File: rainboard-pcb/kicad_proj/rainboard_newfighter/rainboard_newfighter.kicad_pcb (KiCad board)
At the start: 2 copper layers, 260 x 253.6 mm, 595 parts, among them J1 EJ508A, J10 Conn_01x03, J11 SDS-50J, J12 SDS-50J, J13 Conn_01x02, J14 Conn_01x02, J15 Conn_01x02, J16 Conn_01x02, J2 Conn_01x02, J3 Conn_01x03, J4 Conn_01x03, J5 Conn_01x02, J6 Conn_01x02, J6 SDS-50J, J7 Conn_01x02, J7 SDS-50J, J8 Conn_01x02, Q1 DUAL 30V NMOS, Q2 DUAL 30V NMOS, Q3 30V 10mOhm, U1 RT8298, U2 ATmega16U2-MU, U3 6N138SDM, U4 74HC14, U5 ATmega16U2-MU, U6 ATmega2560-16AU, Y1 16MHz, Y1 Crystal, Y2 16MHz, Y2 Crystal, Y3 16MHz

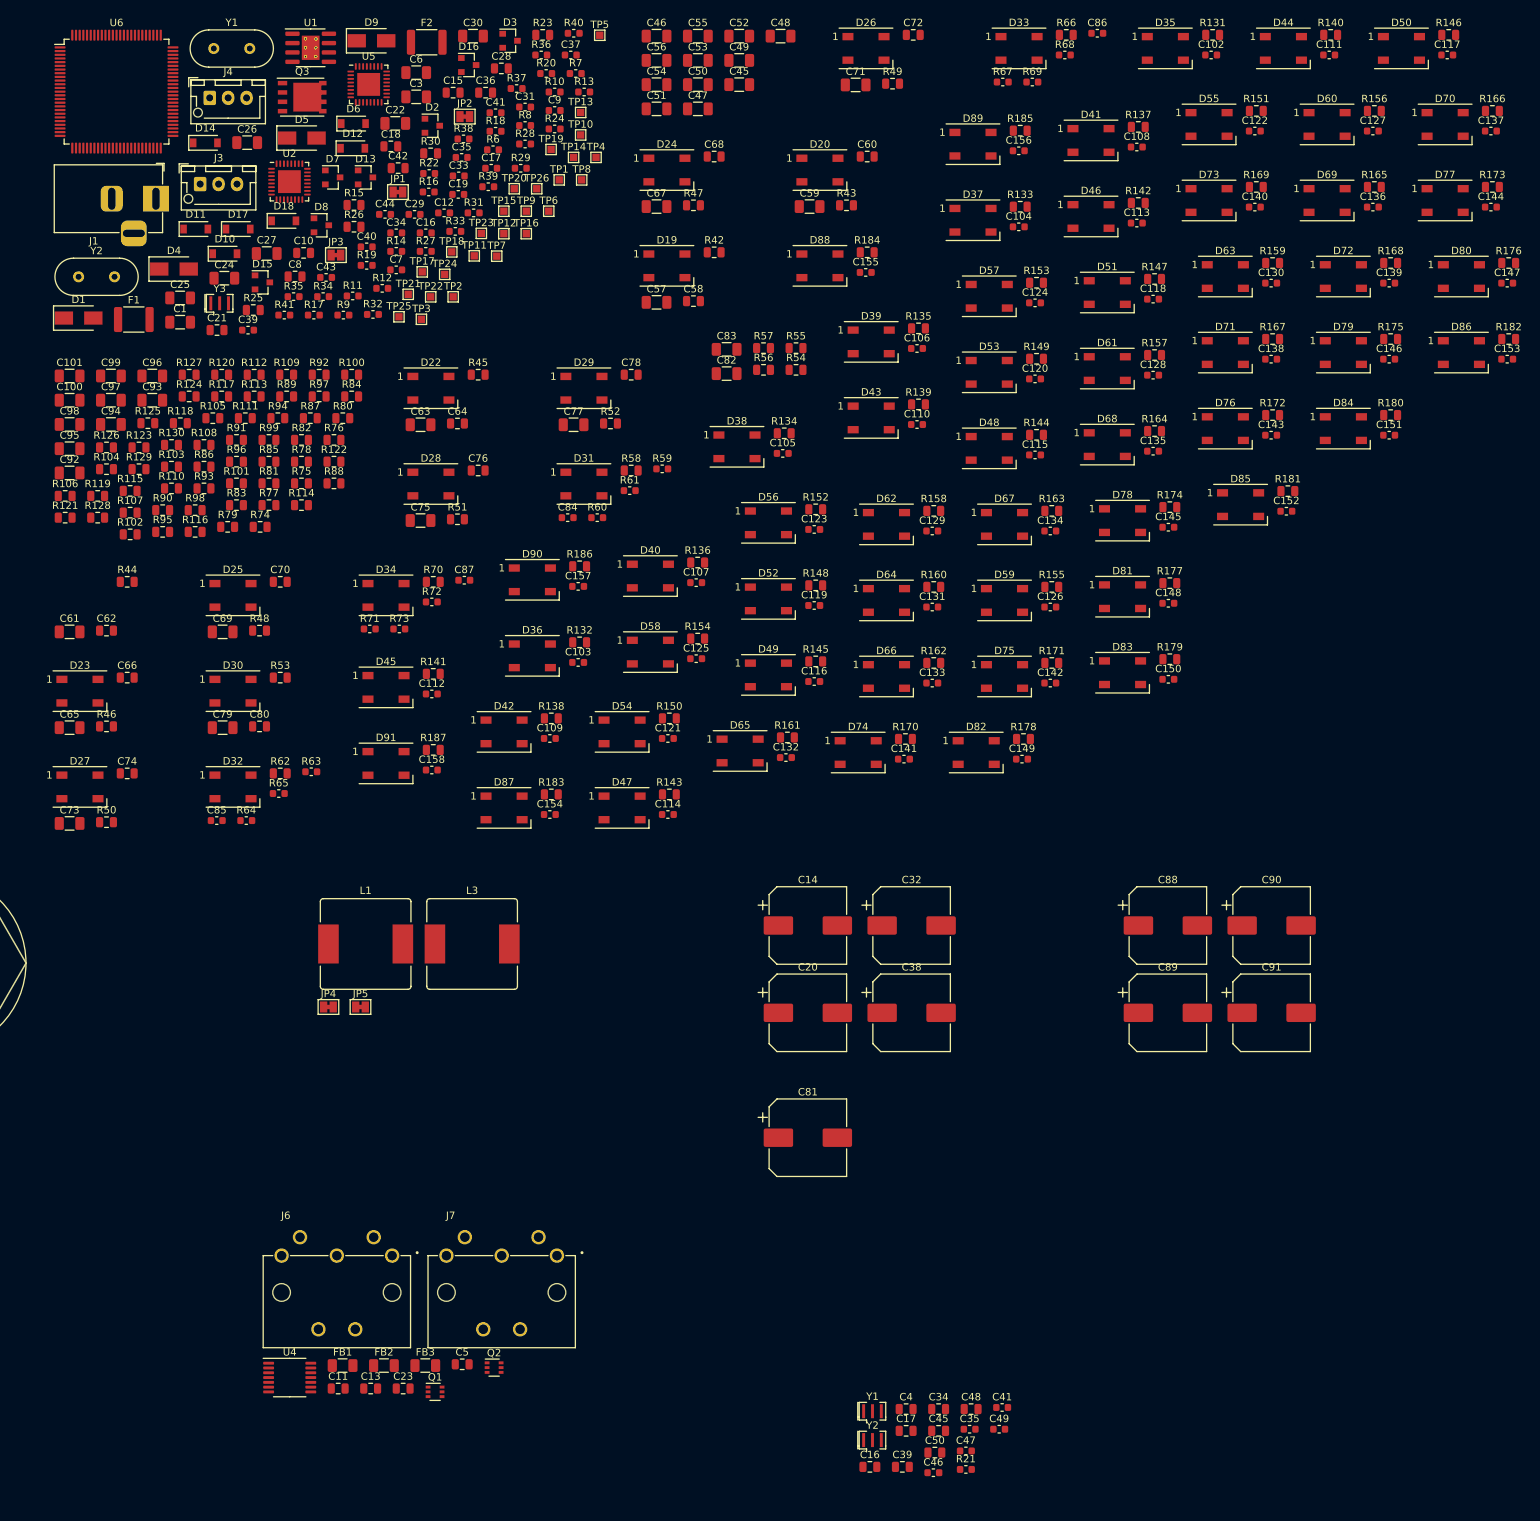
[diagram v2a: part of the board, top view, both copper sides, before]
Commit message: New footprints added
Updated library format for footprints. Pending sync with layout to add all new footprints
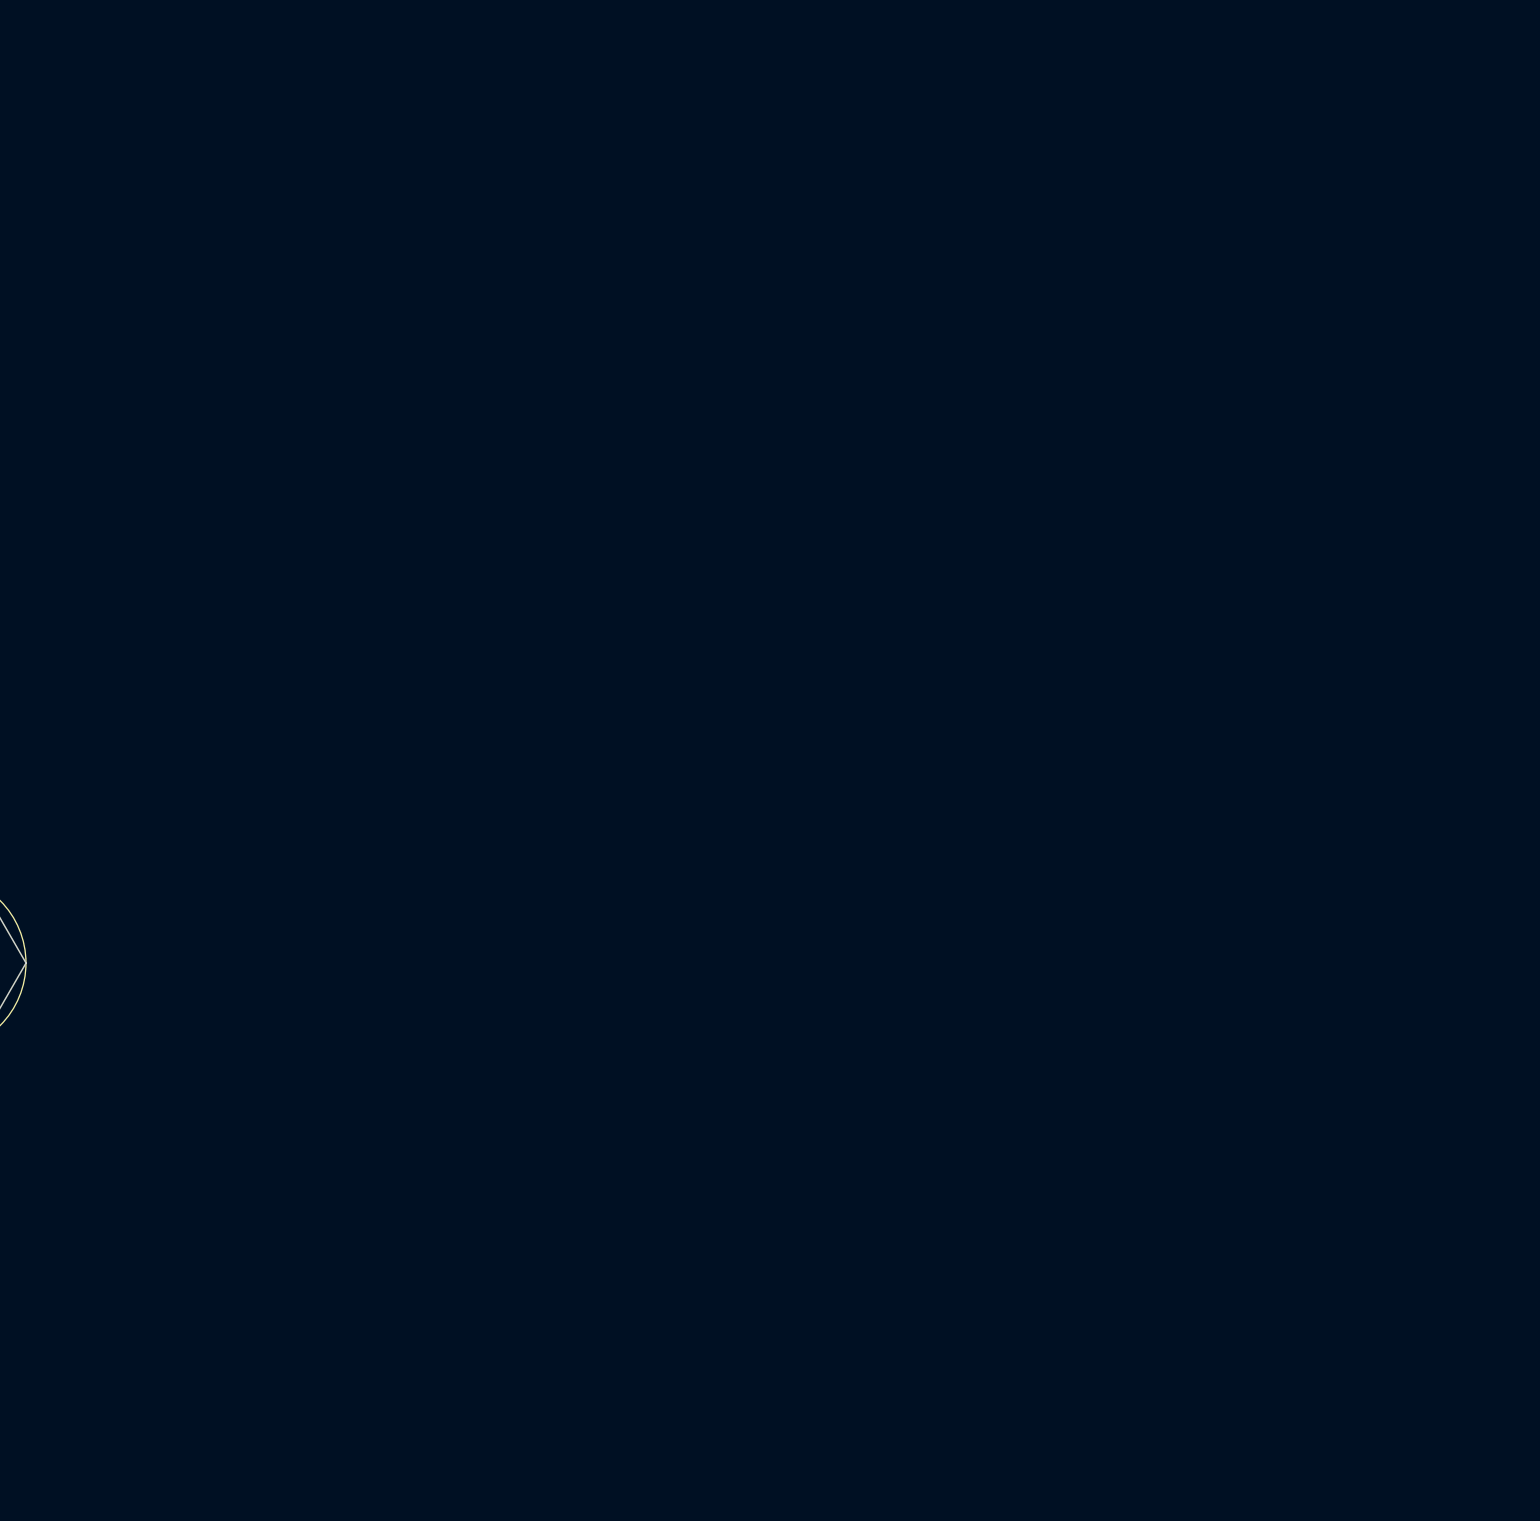
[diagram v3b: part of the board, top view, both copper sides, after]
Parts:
- removed the C1 at (150.9, -87.0)
- removed C10, C11, C13, C15, C17, C18, C21, C23, C28, C34, C36, C39, C42, C45, C48, C5, C50, C58, C60, C62, C64, C66, C68, C70, C72, C74, C76, C78, C8, C80: 1uF 25V, Capacitor_SMD:C_0805_2012Metric
- removed C100, C101, C22, C24, C25, C26, C27, C30, C45, C46, C47, C48, C49, C50, C51, C52, C53, C54, C55, C56, C6, C82, C83, C92, C93, C94, C95, C96, C97, C98, C99: 10uF 25V, Capacitor_SMD:C_1206_3216Metric
- removed C102, C103, C104, C105, C106, C107, C108, C109, C110, C111, C112, C113, C114, C115, C116, C117, C118, C119, C12, C120, C121, C122, C123, C124, C125, C126, C127, C128, C129, C130, C131, C132, C133, C134, C135, C136, C137, C138, C139, C140, C141, C142, C143, C144, C145, C146, C147, C148, C149, C150, C151, C152, C153, C154, C155, C156, C157, C158, C19, C29, C31, C33, C35, C37, C39, C40, C41 (x2), C43, C44, C46, C47, C49, C7, C84, C85, C86, C87, C9: 100nf, Capacitor_SMD:C_0603_1608Metric
- removed C14, C20, C32, C38, C81, C88, C89, C90, C91: 470uF 25V, Capacitor_SMD:CP_Elec_10x10
- removed C16: DNP-1uF 25V, Capacitor_SMD:C_0805_2012Metric
- removed C16, C17, C34, C35: 22PF, Capacitor_SMD:C_0603_1608Metric
- removed the C3 at (182.9, -117.6)
- removed the C4 at (249.4, 60.5)
- removed C57, C59, C61, C63, C65, C67, C69, C71, C73, C75, C77, C79: DNP-10uF 25V, Capacitor_SMD:C_1206_3216Metric
- removed the D1 at (137.1, -87.5)
- removed D10, D11, D12, D14, D17, D18, D6: 40V 1A, Diode_SMD:D_SOD-123
- removed D13, D15, D16, D2, D3, D7, D8: 5Vw, Package_TO_SOT_SMD:SOT-23
- removed D19, D20, D22, D23, D24, D25, D26, D27, D28, D29, D30, D31, D32, D33, D34, D35, D36, D37, D38, D39, D40, D41, D42, D43, D44, D45, D46, D47, D48, D49, D50, D51, D52, D53, D54, D55, D56, D57, D58, D59, D60, D61, D62, D63, D64, D65, D66, D67, D68, D69, D70, D71, D72, D73, D74, D75, D76, D77, D78, D79, D80, D81, D82, D83, D84, D85, D86, D87, D88, D89, D90, D91: WS2812B, LED_SMD:LED_WS2812B_PLCC4_5.0x5.0mm_P3.2mm
- removed D4, D9: 5Vw, Diode_SMD:D_SMA
- removed D5: 12Vw, Diode_SMD:D_SMA
- removed F1: 20V 3A, Fuse:Fuse_1812_4532Metric
- removed F2: 15V .5A, Fuse:Fuse_1812_4532Metric
- removed FB1, FB2, FB3: 4A Ferrite, Inductor_SMD:L_1206_3216Metric
- removed the J1 at (147.6, -103.7)
- removed the J3 at (153.6, -105.7)
- removed the J4 at (154.9, -117.4)
- removed the J6 at (172.2, 39.7)
- removed the J7 at (194.5, 39.7)
- removed JP1, JP2, JP3, JP4, JP5: Jumper, Jumper:SolderJumper-2_P1.3mm_Bridged_Pad1.0x1.5mm
- removed L1, L3: 27uH, Inductor_SMD:L_Bourns_SRR1210A
- removed Q1, Q2: DUAL 30V NMOS, Package_TO_SOT_SMD:SOT-363_SC-70-6
- removed Q3: 30V 10mOhm, Package_SO:PowerPAK_SO-8_Single
- removed the R10 at (201.7, -118.2)
- removed R100, R101, R102, R103, R104, R105, R106, R107, R108, R109, R110, R111, R112, R113, R114, R115, R116, R117, R118, R119, R120, R121, R122, R123, R124, R125, R126, R127, R128, R129, R130, R131, R132, R133, R134, R135, R136, R137, R138, R139, R140, R141, R142, R143, R144, R145, R146, R147, R148, R149, R15, R150, R151, R152, R153, R154, R155, R156, R157, R158, R159, R160, R161, R162, R163, R164, R165, R166, R167, R168, R169, R170, R171, R172, R173, R174, R175, R176, R177, R178, R179, R180, R181, R182, R183, R184, R185, R186, R187, R23, R25, R30, R54, R55, R56, R57, R58, R62, R66, R70, R74, R75, R76, R77, R78, R79, R80, R81, R82, R83, R84, R85, R86, R87, R88, R89, R90, R91, R92, R93, R94, R95, R96, R97, R98, R99: 210R, Resistor_SMD:R_0805_2012Metric
- removed the R11 at (174.3, -90.5)
- removed R12, R14, R16: 100k, Resistor_SMD:R_0603_1608Metric
- removed R13, R24, R27, R28, R34, R40, R60, R61, R64, R65, R68, R69, R72, R73: 19.1k, Resistor_SMD:R_0603_1608Metric
- removed R17, R20, R22, R29, R31, R36, R37, R38, R39, R8: 11R, Resistor_SMD:R_0603_1608Metric
- removed R18: DNP-4.7k, Resistor_SMD:R_0603_1608Metric
- removed R19, R32, R33, R35, R41, R59, R63, R67, R71: 4.7k, Resistor_SMD:R_0603_1608Metric
- removed the R21 at (257.5, 68.7)
- removed R26: DNP-210R, Resistor_SMD:R_0805_2012Metric
- removed R42, R43, R44, R45, R46, R47, R48, R49, R50, R51, R52, R53: 220R, Resistor_SMD:R_0805_2012Metric
- removed the R6 at (193.4, -110.4)
- removed the R7 at (204.6, -120.7)
- removed the R9 at (173.1, -87.9)
- removed TP1, TP10, TP11, TP12, TP13, TP14, TP15, TP16, TP17, TP18, TP19, TP2, TP20, TP21, TP22, TP23, TP24, TP25, TP26, TP3, TP4, TP5, TP6, TP7, TP8, TP9: TestPoint, TestPoint:TestPoint_Pad_1.0x1.0mm
- removed the U1 at (168.6, -124.2)
- removed the U2 at (165.7, -106.0)
- removed U4: 74HC14, Package_SO:TSSOP-14_4.4x5mm_P0.65mm
- removed U5: ATmega16U2-MU, Package_DFN_QFN:QFN-32-1EP_5x5mm_P0.5mm_EP3.1x3.1mm
- removed U6: ATmega2560-16AU, Package_QFP:TQFP-100_14x14mm_P0.5mm
- removed Y1, Y2, Y3: 16MHz, Crystal:Resonator_SMD_muRata_CSTxExxV-3Pin_3.0x1.1mm
- removed Y1, Y2: Crystal, Crystal:Crystal_HC49-U_Vertical

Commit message: Fixing annotations for buttons and meta buttons
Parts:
- removed D21: WS2812B, LED_SMD:LED_WS2812B_PLCC4_5.0x5.0mm_P3.2mm
- removed Je: Conn_01x03, Connector_JST:JST_XH_B3B-XH-AM_1x03_P2.50mm_Vertical
- removed XA1: Arduino_Mega2560_Shield, arduno_mega:Arduino_Mega2560_Shield
- added C10: 1uF 25V, Capacitor_SMD:C_0805_2012Metric, F.Cu at (258.8, -59.7)
- added C100: 10uF 25V, Capacitor_SMD:C_1206_3216Metric, F.Cu at (169.3, 8.35)
- added C101: 10uF 25V, Capacitor_SMD:C_1206_3216Metric, F.Cu at (175.0, 5.06)
- added C102: 100nf, Capacitor_SMD:C_0603_1608Metric, F.Cu at (330.4, 11.5)
- added C103: 100nf, Capacitor_SMD:C_0603_1608Metric, F.Cu at (412.2, -47.7)
- added C104: 100nf, Capacitor_SMD:C_0603_1608Metric, F.Cu at (380.7, -18.1)
- added C105: 100nf, Capacitor_SMD:C_0603_1608Metric, F.Cu at (218.6, 129.4)
- added C106: 100nf, Capacitor_SMD:C_0603_1608Metric, F.Cu at (268.9, 93.5)
- added C107: 100nf, Capacitor_SMD:C_0603_1608Metric, F.Cu at (462.5, -77.3)
- added C108: 100nf, Capacitor_SMD:C_0603_1608Metric, F.Cu at (319.2, 41.1)
- added C109: 100nf, Capacitor_SMD:C_0603_1608Metric, F.Cu at (380.7, 11.5)
- added C11: 1uF 25V, Capacitor_SMD:C_0805_2012Metric, F.Cu at (234.3, -34.9)
- added C110: 100nf, Capacitor_SMD:C_0603_1608Metric, F.Cu at (319.2, 70.7)
- added C111: 100nf, Capacitor_SMD:C_0603_1608Metric, F.Cu at (268.9, 123.1)
- added C112: 100nf, Capacitor_SMD:C_0603_1608Metric, F.Cu at (462.5, -47.7)
- added C113: 100nf, Capacitor_SMD:C_0603_1608Metric, F.Cu at (168.3, 40.6)
- added C114: 100nf, Capacitor_SMD:C_0603_1608Metric, F.Cu at (431.0, -18.1)
- added C115: 100nf, Capacitor_SMD:C_0603_1608Metric, F.Cu at (512.8, -77.3)
- added C116: 100nf, Capacitor_SMD:C_0603_1608Metric, F.Cu at (319.2, 100.3)
- added C117: 100nf, Capacitor_SMD:C_0603_1608Metric, F.Cu at (431.0, 11.5)
- added C118: 100nf, Capacitor_SMD:C_0603_1608Metric, F.Cu at (369.5, 70.7)
- added C119: 100nf, Capacitor_SMD:C_0603_1608Metric, F.Cu at (512.8, -47.7)
- added C12: 100nf, Capacitor_SMD:C_0603_1608Metric, F.Cu at (225.1, -19.6)
- added C120: 100nf, Capacitor_SMD:C_0603_1608Metric, F.Cu at (319.2, 129.9)
- added C121: 100nf, Capacitor_SMD:C_0603_1608Metric, F.Cu at (481.3, -18.1)
- added C122: 100nf, Capacitor_SMD:C_0603_1608Metric, F.Cu at (419.8, 41.1)
- added C123: 100nf, Capacitor_SMD:C_0603_1608Metric, F.Cu at (563.1, -77.3)
- added C124: 100nf, Capacitor_SMD:C_0603_1608Metric, F.Cu at (369.5, 100.3)
- added C125: 100nf, Capacitor_SMD:C_0603_1608Metric, F.Cu at (481.3, 11.5)
- added C126: 100nf, Capacitor_SMD:C_0603_1608Metric, F.Cu at (419.8, 70.7)
- added C127: 100nf, Capacitor_SMD:C_0603_1608Metric, F.Cu at (563.1, -47.7)
- added C128: 100nf, Capacitor_SMD:C_0603_1608Metric, F.Cu at (369.5, 41.1)
- added C129: 100nf, Capacitor_SMD:C_0603_1608Metric, F.Cu at (470.1, 41.1)
- added C13: 1uF 25V, Capacitor_SMD:C_0805_2012Metric, F.Cu at (238.8, -37.9)
- added C130: 100nf, Capacitor_SMD:C_0603_1608Metric, F.Cu at (531.6, -18.1)
- added C131: 100nf, Capacitor_SMD:C_0603_1608Metric, F.Cu at (419.8, 100.3)
- added C132: 100nf, Capacitor_SMD:C_0603_1608Metric, F.Cu at (531.6, 11.5)
- added C133: 100nf, Capacitor_SMD:C_0603_1608Metric, F.Cu at (470.1, 70.7)
- added C134: 100nf, Capacitor_SMD:C_0603_1608Metric, F.Cu at (419.8, 129.9)
- added C135: 100nf, Capacitor_SMD:C_0603_1608Metric, F.Cu at (520.4, 41.1)
- added C136: 100nf, Capacitor_SMD:C_0603_1608Metric, F.Cu at (470.1, 100.3)
- added C137: 100nf, Capacitor_SMD:C_0603_1608Metric, F.Cu at (520.4, 70.7)
- added C138: 100nf, Capacitor_SMD:C_0603_1608Metric, F.Cu at (470.1, 129.9)
- added C139: 100nf, Capacitor_SMD:C_0603_1608Metric, F.Cu at (570.6, 41.1)
- added C14: 470uF 25V, Capacitor_SMD:CP_Elec_10x10, F.Cu at (231.8, -72.6)
- added C140: 100nf, Capacitor_SMD:C_0603_1608Metric, F.Cu at (520.4, 100.3)
- added C141: 100nf, Capacitor_SMD:C_0603_1608Metric, F.Cu at (570.6, 70.7)
- added C142: 100nf, Capacitor_SMD:C_0603_1608Metric, F.Cu at (369.5, 129.9)
- added C143: 100nf, Capacitor_SMD:C_0603_1608Metric, F.Cu at (311.7, -77.3)
- added C144: 100nf, Capacitor_SMD:C_0603_1608Metric, F.Cu at (229.9, 4.67)
- added C145: 100nf, Capacitor_SMD:C_0603_1608Metric, F.Cu at (311.7, -47.7)
- added C146: 100nf, Capacitor_SMD:C_0603_1608Metric, F.Cu at (218.6, 40.6)
- added C147: 100nf, Capacitor_SMD:C_0603_1608Metric, F.Cu at (168.3, 70.2)
- added C148: 100nf, Capacitor_SMD:C_0603_1608Metric, F.Cu at (361.9, -77.3)
- added C149: 100nf, Capacitor_SMD:C_0603_1608Metric, F.Cu at (168.3, 99.8)
- added C15: 1uF 25V, Capacitor_SMD:C_0805_2012Metric, F.Cu at (223.4, -27.9)
- added C150: 100nf, Capacitor_SMD:C_0603_1608Metric, F.Cu at (280.2, 4.67)
- added C151: 100nf, Capacitor_SMD:C_0603_1608Metric, F.Cu at (218.6, 70.2)
- added C152: 100nf, Capacitor_SMD:C_0603_1608Metric, F.Cu at (361.9, -47.7)
- added C153: 100nf, Capacitor_SMD:C_0603_1608Metric, F.Cu at (168.3, 129.4)
- added C154: 100nf, Capacitor_SMD:C_0603_1608Metric, F.Cu at (268.9, 34.3)
- added C155: 100nf, Capacitor_SMD:C_0603_1608Metric, F.Cu at (412.2, -77.3)
- added C156: 100nf, Capacitor_SMD:C_0603_1608Metric, F.Cu at (268.9, 63.9)
- added C157: 100nf, Capacitor_SMD:C_0603_1608Metric, F.Cu at (218.6, 99.8)
- added C158: 100nf, Capacitor_SMD:C_0603_1608Metric, F.Cu at (330.4, -18.1)
- added C16: DNP-1uF 25V, Capacitor_SMD:C_0805_2012Metric, F.Cu at (233.8, -31.3)
- added C17: 1uF 25V, Capacitor_SMD:C_0805_2012Metric, F.Cu at (220.9, -21.3)
- added C18: 1uF 25V, Capacitor_SMD:C_0805_2012Metric, F.Cu at (247.7, -47.0)
- added C19: 100nf, Capacitor_SMD:C_0603_1608Metric, F.Cu at (213.2, -9.86)
- added C20: 470uF 25V, Capacitor_SMD:CP_Elec_10x10, F.Cu at (165.2, -17.3)
- added C21: 1uF 25V, Capacitor_SMD:C_0805_2012Metric, F.Cu at (215.7, -15.1)
- added C22: 10uF 25V, Capacitor_SMD:C_1206_3216Metric, F.Cu at (249.3, -56.0)
- added C23: 1uF 25V, Capacitor_SMD:C_0805_2012Metric, F.Cu at (258.8, -56.8)
- added C24: 10uF 25V, Capacitor_SMD:C_1206_3216Metric, F.Cu at (236.5, -44.5)
- added C25: 10uF 25V, Capacitor_SMD:C_1206_3216Metric, F.Cu at (249.3, -59.3)
- added C26: 10uF 25V, Capacitor_SMD:C_1206_3216Metric, F.Cu at (224.4, -34.9)
- added C27: 10uF 25V, Capacitor_SMD:C_1206_3216Metric, F.Cu at (218.4, -27.7)
- added C28: 1uF 25V, Capacitor_SMD:C_0805_2012Metric, F.Cu at (199.1, -36.6)
- added C29: 100nf, Capacitor_SMD:C_0603_1608Metric, F.Cu at (263.0, -57.9)
- added C30: 10uF 25V, Capacitor_SMD:C_1206_3216Metric, F.Cu at (224.4, -31.6)
- added C31: 100nf, Capacitor_SMD:C_0603_1608Metric, F.Cu at (232.0, -26.1)
- added C32: 470uF 25V, Capacitor_SMD:CP_Elec_10x10, F.Cu at (179.3, -15.7)
- added C33: 100nf, Capacitor_SMD:C_0603_1608Metric, F.Cu at (217.4, -35.3)
- added C34: 1uF 25V, Capacitor_SMD:C_0805_2012Metric, F.Cu at (247.7, -49.9)
- added C35: 100nf, Capacitor_SMD:C_0603_1608Metric, F.Cu at (216.7, -12.4)
- added C36: 1uF 25V, Capacitor_SMD:C_0805_2012Metric, F.Cu at (260.4, -62.7)
- added C37: 100nf, Capacitor_SMD:C_0603_1608Metric, F.Cu at (238.6, -35.2)
- added C38: 470uF 25V, Capacitor_SMD:CP_Elec_10x10, F.Cu at (208.7, -39.8)
- added C39: 1uF 25V, Capacitor_SMD:C_0805_2012Metric, F.Cu at (229.4, -31.3)
- added C40: 100nf, Capacitor_SMD:C_0603_1608Metric, F.Cu at (232.0, -28.6)
- added C41: 100nf, Capacitor_SMD:C_0603_1608Metric, F.Cu at (203.3, -0.98)
- added C42: 1uF 25V, Capacitor_SMD:C_0805_2012Metric, F.Cu at (204.6, -6.66)
- added C43: 100nf, Capacitor_SMD:C_0603_1608Metric, F.Cu at (251.9, -47.2)
- added C44: 100nf, Capacitor_SMD:C_0603_1608Metric, F.Cu at (243.0, -38.6)
- added C45: 1uF 25V, Capacitor_SMD:C_0805_2012Metric, F.Cu at (223.4, -24.9)
- added C46: 100nf, Capacitor_SMD:C_0603_1608Metric, F.Cu at (256.3, -50.1)
- added C47: 100nf, Capacitor_SMD:C_0603_1608Metric, F.Cu at (212.7, -12.4)
- added C48: 1uF 25V, Capacitor_SMD:C_0805_2012Metric, F.Cu at (208.5, -12.4)
- added C49: 100nf, Capacitor_SMD:C_0603_1608Metric, F.Cu at (238.6, -32.6)
- added C5: 1uF 25V, Capacitor_SMD:C_0805_2012Metric, F.Cu at (252.1, -49.9)
- added C50: 1uF 25V, Capacitor_SMD:C_0805_2012Metric, F.Cu at (252.2, -52.9)
- added C6: 10uF 25V, Capacitor_SMD:C_1206_3216Metric, F.Cu at (211.4, -19.5)
- added C7: 100nf, Capacitor_SMD:C_0603_1608Metric, F.Cu at (219.9, -15.0)
- added C8: 1uF 25V, Capacitor_SMD:C_0805_2012Metric, F.Cu at (268.8, -68.0)
- added C88: 470uF 25V, Capacitor_SMD:CP_Elec_10x10, F.Cu at (140.1, 9.34)
- added C89: 470uF 25V, Capacitor_SMD:CP_Elec_10x10, F.Cu at (140.1, 21.2)
- added C9: 100nf, Capacitor_SMD:C_0603_1608Metric, F.Cu at (213.2, -7.35)
- added C90: 470uF 25V, Capacitor_SMD:CP_Elec_10x10, F.Cu at (154.2, 21.2)
- added C91: 470uF 25V, Capacitor_SMD:CP_Elec_10x10, F.Cu at (154.2, 9.34)
- added C92: 10uF 25V, Capacitor_SMD:C_1206_3216Metric, F.Cu at (163.7, 5.06)
- added C93: 10uF 25V, Capacitor_SMD:C_1206_3216Metric, F.Cu at (135.6, 32.0)
- added C94: 10uF 25V, Capacitor_SMD:C_1206_3216Metric, F.Cu at (141.2, 28.8)
- added C95: 10uF 25V, Capacitor_SMD:C_1206_3216Metric, F.Cu at (141.2, 32.0)
- added C96: 10uF 25V, Capacitor_SMD:C_1206_3216Metric, F.Cu at (169.3, 5.06)
- added C97: 10uF 25V, Capacitor_SMD:C_1206_3216Metric, F.Cu at (163.7, 8.35)
- added C98: 10uF 25V, Capacitor_SMD:C_1206_3216Metric, F.Cu at (163.7, 11.6)
- added C99: 10uF 25V, Capacitor_SMD:C_1206_3216Metric, F.Cu at (135.6, 28.8)
- added D10: 40V 1A, Diode_SMD:D_SOD-123, F.Cu at (183.1, -41.0)
- added D11: 40V 1A, Diode_SMD:D_SOD-123, F.Cu at (135.7, -1.49)
- added D12: 40V 1A, Diode_SMD:D_SOD-123, F.Cu at (152.9, -1.49)
- added D13: 5Vw, Package_TO_SOT_SMD:SOT-23, F.Cu at (216.4, -18.9)
- added D14: 40V 1A, Diode_SMD:D_SOD-123, F.Cu at (147.2, -1.49)
- added D15: 5Vw, Package_TO_SOT_SMD:SOT-23, F.Cu at (242.9, -46.0)
- added D16: 5Vw, Package_TO_SOT_SMD:SOT-23, F.Cu at (199.1, -2.06)
- added D17: 40V 1A, Diode_SMD:D_SOD-123, F.Cu at (183.1, -37.6)
- added D18: 40V 1A, Diode_SMD:D_SOD-123, F.Cu at (250.9, -62.6)
- added D2: 5Vw, Package_TO_SOT_SMD:SOT-23, F.Cu at (199.1, -40.4)
- added D3: 5Vw, Package_TO_SOT_SMD:SOT-23, F.Cu at (254.3, -58.6)
- added D35: WS2812B, LED_SMD:LED_WS2812B_PLCC4_5.0x5.0mm_P3.2mm, F.Cu at (324.2, 13.6)
- added D36: WS2812B, LED_SMD:LED_WS2812B_PLCC4_5.0x5.0mm_P3.2mm, F.Cu at (406.0, -45.6)
- added D37: WS2812B, LED_SMD:LED_WS2812B_PLCC4_5.0x5.0mm_P3.2mm, F.Cu at (374.5, -16.0)
- added D38: WS2812B, LED_SMD:LED_WS2812B_PLCC4_5.0x5.0mm_P3.2mm, F.Cu at (212.4, 131.5)
- added D39: WS2812B, LED_SMD:LED_WS2812B_PLCC4_5.0x5.0mm_P3.2mm, F.Cu at (262.7, 95.5)
- added D4: 5Vw, Diode_SMD:D_SMA, F.Cu at (264.0, -76.2)
- added D40: WS2812B, LED_SMD:LED_WS2812B_PLCC4_5.0x5.0mm_P3.2mm, F.Cu at (456.3, -75.2)
- added D41: WS2812B, LED_SMD:LED_WS2812B_PLCC4_5.0x5.0mm_P3.2mm, F.Cu at (313.0, 43.2)
- added D42: WS2812B, LED_SMD:LED_WS2812B_PLCC4_5.0x5.0mm_P3.2mm, F.Cu at (374.5, 13.6)
- added D43: WS2812B, LED_SMD:LED_WS2812B_PLCC4_5.0x5.0mm_P3.2mm, F.Cu at (313.0, 72.8)
- added D44: WS2812B, LED_SMD:LED_WS2812B_PLCC4_5.0x5.0mm_P3.2mm, F.Cu at (262.7, 125.1)
- added D45: WS2812B, LED_SMD:LED_WS2812B_PLCC4_5.0x5.0mm_P3.2mm, F.Cu at (456.3, -45.6)
- added D46: WS2812B, LED_SMD:LED_WS2812B_PLCC4_5.0x5.0mm_P3.2mm, F.Cu at (162.1, 42.7)
- added D47: WS2812B, LED_SMD:LED_WS2812B_PLCC4_5.0x5.0mm_P3.2mm, F.Cu at (424.8, -16.0)
- added D48: WS2812B, LED_SMD:LED_WS2812B_PLCC4_5.0x5.0mm_P3.2mm, F.Cu at (506.6, -75.2)
- added D49: WS2812B, LED_SMD:LED_WS2812B_PLCC4_5.0x5.0mm_P3.2mm, F.Cu at (313.0, 102.4)
- added D5: 12Vw, Diode_SMD:D_SMA, F.Cu at (229.6, -42.2)
- added D50: WS2812B, LED_SMD:LED_WS2812B_PLCC4_5.0x5.0mm_P3.2mm, F.Cu at (424.8, 13.6)
- added D51: WS2812B, LED_SMD:LED_WS2812B_PLCC4_5.0x5.0mm_P3.2mm, F.Cu at (363.3, 72.8)
- added D52: WS2812B, LED_SMD:LED_WS2812B_PLCC4_5.0x5.0mm_P3.2mm, F.Cu at (506.6, -45.6)
- added D53: WS2812B, LED_SMD:LED_WS2812B_PLCC4_5.0x5.0mm_P3.2mm, F.Cu at (313.0, 132.0)
- added D54: WS2812B, LED_SMD:LED_WS2812B_PLCC4_5.0x5.0mm_P3.2mm, F.Cu at (475.1, -16.0)
- added D55: WS2812B, LED_SMD:LED_WS2812B_PLCC4_5.0x5.0mm_P3.2mm, F.Cu at (413.6, 43.2)
- added D56: WS2812B, LED_SMD:LED_WS2812B_PLCC4_5.0x5.0mm_P3.2mm, F.Cu at (556.9, -75.2)
- added D57: WS2812B, LED_SMD:LED_WS2812B_PLCC4_5.0x5.0mm_P3.2mm, F.Cu at (363.3, 102.4)
- added D58: WS2812B, LED_SMD:LED_WS2812B_PLCC4_5.0x5.0mm_P3.2mm, F.Cu at (475.1, 13.6)
- added D59: WS2812B, LED_SMD:LED_WS2812B_PLCC4_5.0x5.0mm_P3.2mm, F.Cu at (413.6, 72.8)
- added D6: 40V 1A, Diode_SMD:D_SOD-123, F.Cu at (141.4, -1.49)
- added D60: WS2812B, LED_SMD:LED_WS2812B_PLCC4_5.0x5.0mm_P3.2mm, F.Cu at (556.9, -45.6)
- added D61: WS2812B, LED_SMD:LED_WS2812B_PLCC4_5.0x5.0mm_P3.2mm, F.Cu at (363.3, 43.2)
- added D62: WS2812B, LED_SMD:LED_WS2812B_PLCC4_5.0x5.0mm_P3.2mm, F.Cu at (463.8, 43.2)
- added D63: WS2812B, LED_SMD:LED_WS2812B_PLCC4_5.0x5.0mm_P3.2mm, F.Cu at (525.4, -16.0)
- added D64: WS2812B, LED_SMD:LED_WS2812B_PLCC4_5.0x5.0mm_P3.2mm, F.Cu at (413.6, 102.4)
- added D65: WS2812B, LED_SMD:LED_WS2812B_PLCC4_5.0x5.0mm_P3.2mm, F.Cu at (525.4, 13.6)
- added D66: WS2812B, LED_SMD:LED_WS2812B_PLCC4_5.0x5.0mm_P3.2mm, F.Cu at (463.8, 72.8)
- added D67: WS2812B, LED_SMD:LED_WS2812B_PLCC4_5.0x5.0mm_P3.2mm, F.Cu at (413.6, 132.0)
- added D68: WS2812B, LED_SMD:LED_WS2812B_PLCC4_5.0x5.0mm_P3.2mm, F.Cu at (514.1, 43.2)
- added D69: WS2812B, LED_SMD:LED_WS2812B_PLCC4_5.0x5.0mm_P3.2mm, F.Cu at (463.8, 102.4)
- added D7: 5Vw, Package_TO_SOT_SMD:SOT-23, F.Cu at (269.1, -71.7)
- added D70: WS2812B, LED_SMD:LED_WS2812B_PLCC4_5.0x5.0mm_P3.2mm, F.Cu at (514.1, 72.8)
- added D71: WS2812B, LED_SMD:LED_WS2812B_PLCC4_5.0x5.0mm_P3.2mm, F.Cu at (463.8, 132.0)
- added D72: WS2812B, LED_SMD:LED_WS2812B_PLCC4_5.0x5.0mm_P3.2mm, F.Cu at (564.4, 43.2)
- added D73: WS2812B, LED_SMD:LED_WS2812B_PLCC4_5.0x5.0mm_P3.2mm, F.Cu at (514.1, 102.4)
- added D74: WS2812B, LED_SMD:LED_WS2812B_PLCC4_5.0x5.0mm_P3.2mm, F.Cu at (564.4, 72.8)
- added D75: WS2812B, LED_SMD:LED_WS2812B_PLCC4_5.0x5.0mm_P3.2mm, F.Cu at (363.3, 132.0)
- added D76: WS2812B, LED_SMD:LED_WS2812B_PLCC4_5.0x5.0mm_P3.2mm, F.Cu at (305.4, -75.2)
- added D77: WS2812B, LED_SMD:LED_WS2812B_PLCC4_5.0x5.0mm_P3.2mm, F.Cu at (223.7, 6.72)
- added D78: WS2812B, LED_SMD:LED_WS2812B_PLCC4_5.0x5.0mm_P3.2mm, F.Cu at (305.4, -45.6)
- added D79: WS2812B, LED_SMD:LED_WS2812B_PLCC4_5.0x5.0mm_P3.2mm, F.Cu at (212.4, 42.7)
- added D8: 5Vw, Package_TO_SOT_SMD:SOT-23, F.Cu at (264.3, -68.2)
- added D80: WS2812B, LED_SMD:LED_WS2812B_PLCC4_5.0x5.0mm_P3.2mm, F.Cu at (162.1, 72.3)
- added D81: WS2812B, LED_SMD:LED_WS2812B_PLCC4_5.0x5.0mm_P3.2mm, F.Cu at (355.7, -75.2)
- added D82: WS2812B, LED_SMD:LED_WS2812B_PLCC4_5.0x5.0mm_P3.2mm, F.Cu at (162.1, 101.9)
- added D83: WS2812B, LED_SMD:LED_WS2812B_PLCC4_5.0x5.0mm_P3.2mm, F.Cu at (273.9, 6.72)
- added D84: WS2812B, LED_SMD:LED_WS2812B_PLCC4_5.0x5.0mm_P3.2mm, F.Cu at (212.4, 72.3)
- added D85: WS2812B, LED_SMD:LED_WS2812B_PLCC4_5.0x5.0mm_P3.2mm, F.Cu at (355.7, -45.6)
- added D86: WS2812B, LED_SMD:LED_WS2812B_PLCC4_5.0x5.0mm_P3.2mm, F.Cu at (162.1, 131.5)
- added D87: WS2812B, LED_SMD:LED_WS2812B_PLCC4_5.0x5.0mm_P3.2mm, F.Cu at (262.7, 36.3)
- added D88: WS2812B, LED_SMD:LED_WS2812B_PLCC4_5.0x5.0mm_P3.2mm, F.Cu at (406.0, -75.2)
- added D89: WS2812B, LED_SMD:LED_WS2812B_PLCC4_5.0x5.0mm_P3.2mm, F.Cu at (262.7, 65.9)
- added D9: 5Vw, Diode_SMD:D_SMA, F.Cu at (241.6, -54.0)
- added D90: WS2812B, LED_SMD:LED_WS2812B_PLCC4_5.0x5.0mm_P3.2mm, F.Cu at (212.4, 101.9)
- added D91: WS2812B, LED_SMD:LED_WS2812B_PLCC4_5.0x5.0mm_P3.2mm, F.Cu at (324.2, -16.0)
- added F1: 20V 3A, Fuse:Fuse_1812_4532Metric, F.Cu at (212.1, -23.6)
- added F2: 15V .5A, Fuse:Fuse_1812_4532Metric, F.Cu at (237.2, -48.6)
- added FB1: 4A Ferrite, Inductor_SMD:L_1206_3216Metric, F.Cu at (218.4, -24.4)
- added FB2: 4A Ferrite, Inductor_SMD:L_1206_3216Metric, F.Cu at (199.6, -5.98)
- added FB3: 4A Ferrite, Inductor_SMD:L_1206_3216Metric, F.Cu at (227.7, -38.3)
- added J17: Conn_01x02_Female, Connector_JST:JST_XH_B2B-XH-A_1x02_P2.50mm_Vertical, F.Cu at (242.1, -67.3)
- added J18: Conn_01x02_Female, Connector_JST:JST_XH_B2B-XH-A_1x02_P2.50mm_Vertical, F.Cu at (231.6, -63.3)
- added J19: Conn_01x02_Female, Connector_JST:JST_XH_B2B-XH-A_1x02_P2.50mm_Vertical, F.Cu at (193.2, -19.9)
- added J20: Conn_01x02_Female, Connector_JST:JST_XH_B2B-XH-A_1x02_P2.50mm_Vertical, F.Cu at (219.6, -48.8)
- added J21: Conn_01x02_Female, Connector_JST:JST_XH_B2B-XH-A_1x02_P2.50mm_Vertical, F.Cu at (174.1, -6.38)
- added J9: PH2-06-UA, Connector_PinHeader_2.54mm:PinHeader_2x03_P2.54mm_Vertical, F.Cu at (192.0, -30.6)
- added JP1: Jumper, Jumper:SolderJumper-2_P1.3mm_Bridged_Pad1.0x1.5mm, F.Cu at (256.6, -53.5)
- added JP2: Jumper, Jumper:SolderJumper-2_P1.3mm_Bridged_Pad1.0x1.5mm, F.Cu at (227.8, -25.1)
- added JP3: Jumper, Jumper:SolderJumper-2_P1.3mm_Bridged_Pad1.0x1.5mm, F.Cu at (209.0, -9.19)
- added JP4: Jumper, Jumper:SolderJumper-2_P1.3mm_Bridged_Pad1.0x1.5mm, F.Cu at (220.8, -18.0)
- added JP5: Jumper, Jumper:SolderJumper-2_P1.3mm_Bridged_Pad1.0x1.5mm, F.Cu at (209.0, -5.64)
- added L1: 27uH, Inductor_SMD:L_12x12mm_H8mm, F.Cu at (208.8, -52.9)
- added L2: 10uH .5Ohm, rainboard_fp:INDC250X180X200L50N, F.Cu at (264.5, -72.2)
- added L3: 27uH, Inductor_SMD:L_12x12mm_H8mm, F.Cu at (182.3, -28.7)
- added L4: 10uH .5Ohm, rainboard_fp:INDC250X180X200L50N, F.Cu at (243.1, -50.0)
- added L5: 10uH .5Ohm, rainboard_fp:INDC250X180X200L50N, F.Cu at (236.0, -41.1)
- added Q1: DUAL 30V NMOS, Package_TO_SOT_SMD:SOT-363_SC-70-6, F.Cu at (264.7, -61.1)
- added Q2: DUAL 30V NMOS, Package_TO_SOT_SMD:SOT-363_SC-70-6, F.Cu at (247.3, -43.6)
- added Q3: 30V 10mOhm, Package_SO:PowerPAK_SO-8_Single, F.Cu at (229.7, -47.8)
- added R100: 210R, Resistor_SMD:R_0805_2012Metric, F.Cu at (167.6, 20.7)
- added R101: 210R, Resistor_SMD:R_0805_2012Metric, F.Cu at (172.0, 17.4)
- added R102: 210R, Resistor_SMD:R_0805_2012Metric, F.Cu at (155.0, 34.5)
- added R103: 210R, Resistor_SMD:R_0805_2012Metric, F.Cu at (183.2, 7.84)
- added R104: 210R, Resistor_SMD:R_0805_2012Metric, F.Cu at (167.6, 17.7)
- added R105: 210R, Resistor_SMD:R_0805_2012Metric, F.Cu at (180.0, 4.89)
- added R106: 210R, Resistor_SMD:R_0805_2012Metric, F.Cu at (168.2, 29.5)
- added R107: 210R, Resistor_SMD:R_0805_2012Metric, F.Cu at (177.6, 11.1)
- added R108: 210R, Resistor_SMD:R_0805_2012Metric, F.Cu at (184.4, 4.89)
- added R109: 210R, Resistor_SMD:R_0805_2012Metric, F.Cu at (172.0, 14.4)
- added R110: 210R, Resistor_SMD:R_0805_2012Metric, F.Cu at (163.1, 23.6)
- added R111: 210R, Resistor_SMD:R_0805_2012Metric, F.Cu at (155.0, 31.5)
- added R112: 210R, Resistor_SMD:R_0805_2012Metric, F.Cu at (178.8, 8.18)
- added R113: 210R, Resistor_SMD:R_0805_2012Metric, F.Cu at (150.6, 34.5)
- added R114: 210R, Resistor_SMD:R_0805_2012Metric, F.Cu at (168.8, 11.5)
- added R115: 210R, Resistor_SMD:R_0805_2012Metric, F.Cu at (173.2, 11.5)
- added R116: 210R, Resistor_SMD:R_0805_2012Metric, F.Cu at (172.7, 29.2)
- added R117: 210R, Resistor_SMD:R_0805_2012Metric, F.Cu at (180.8, 22.9)
- added R118: 210R, Resistor_SMD:R_0805_2012Metric, F.Cu at (177.1, 26.2)
- added R119: 210R, Resistor_SMD:R_0805_2012Metric, F.Cu at (172.7, 32.1)
- added R12: 100k, Resistor_SMD:R_0603_1608Metric, F.Cu at (251.4, -44.2)
- added R120: 210R, Resistor_SMD:R_0805_2012Metric, F.Cu at (185.2, 20.0)
- added R121: 210R, Resistor_SMD:R_0805_2012Metric, F.Cu at (180.8, 17.0)
- added R122: 210R, Resistor_SMD:R_0805_2012Metric, F.Cu at (146.2, 28.6)
- added R123: 210R, Resistor_SMD:R_0805_2012Metric, F.Cu at (180.8, 20.0)
- added R124: 210R, Resistor_SMD:R_0805_2012Metric, F.Cu at (150.6, 28.6)
- added R125: 210R, Resistor_SMD:R_0805_2012Metric, F.Cu at (146.2, 31.5)
- added R126: 210R, Resistor_SMD:R_0805_2012Metric, F.Cu at (174.4, 8.18)
- added R127: 210R, Resistor_SMD:R_0805_2012Metric, F.Cu at (150.6, 31.5)
- added R128: 210R, Resistor_SMD:R_0805_2012Metric, F.Cu at (146.2, 34.5)
- added R129: 210R, Resistor_SMD:R_0805_2012Metric, F.Cu at (167.6, 14.8)
- added R13: 19.1k, Resistor_SMD:R_0603_1608Metric, F.Cu at (220.7, -12.5)
- added R130: 210R, Resistor_SMD:R_0805_2012Metric, F.Cu at (163.1, 17.7)
- added R131: 210R, Resistor_SMD:R_0805_2012Metric, F.Cu at (322.2, 18.4)
- added R132: 210R, Resistor_SMD:R_0805_2012Metric, F.Cu at (404.0, -40.8)
- added R133: 210R, Resistor_SMD:R_0805_2012Metric, F.Cu at (372.5, -11.2)
- added R134: 210R, Resistor_SMD:R_0805_2012Metric, F.Cu at (210.4, 136.2)
- added R135: 210R, Resistor_SMD:R_0805_2012Metric, F.Cu at (260.7, 100.3)
- added R136: 210R, Resistor_SMD:R_0805_2012Metric, F.Cu at (454.3, -70.4)
- added R137: 210R, Resistor_SMD:R_0805_2012Metric, F.Cu at (311.0, 48.0)
- added R138: 210R, Resistor_SMD:R_0805_2012Metric, F.Cu at (372.5, 18.4)
- added R139: 210R, Resistor_SMD:R_0805_2012Metric, F.Cu at (311.0, 77.6)
- added R14: 100k, Resistor_SMD:R_0603_1608Metric, F.Cu at (225.0, -17.0)
- added R140: 210R, Resistor_SMD:R_0805_2012Metric, F.Cu at (260.7, 129.9)
- added R141: 210R, Resistor_SMD:R_0805_2012Metric, F.Cu at (454.3, -40.8)
- added R142: 210R, Resistor_SMD:R_0805_2012Metric, F.Cu at (160.1, 47.5)
- added R143: 210R, Resistor_SMD:R_0805_2012Metric, F.Cu at (422.8, -11.2)
- added R144: 210R, Resistor_SMD:R_0805_2012Metric, F.Cu at (504.6, -70.4)
- added R145: 210R, Resistor_SMD:R_0805_2012Metric, F.Cu at (311.0, 107.2)
- added R146: 210R, Resistor_SMD:R_0805_2012Metric, F.Cu at (422.8, 18.4)
- added R147: 210R, Resistor_SMD:R_0805_2012Metric, F.Cu at (361.3, 77.6)
- added R148: 210R, Resistor_SMD:R_0805_2012Metric, F.Cu at (504.6, -40.8)
- added R149: 210R, Resistor_SMD:R_0805_2012Metric, F.Cu at (311.0, 136.8)
- added R15: 210R, Resistor_SMD:R_0805_2012Metric, F.Cu at (247.8, -52.9)
- added R150: 210R, Resistor_SMD:R_0805_2012Metric, F.Cu at (473.1, -11.2)
- added R151: 210R, Resistor_SMD:R_0805_2012Metric, F.Cu at (411.6, 48.0)
- added R152: 210R, Resistor_SMD:R_0805_2012Metric, F.Cu at (554.9, -70.4)
- added R153: 210R, Resistor_SMD:R_0805_2012Metric, F.Cu at (361.3, 107.2)
- added R154: 210R, Resistor_SMD:R_0805_2012Metric, F.Cu at (473.1, 18.4)
- added R155: 210R, Resistor_SMD:R_0805_2012Metric, F.Cu at (411.6, 77.6)
- added R156: 210R, Resistor_SMD:R_0805_2012Metric, F.Cu at (554.9, -40.8)
- added R157: 210R, Resistor_SMD:R_0805_2012Metric, F.Cu at (361.3, 48.0)
- added R158: 210R, Resistor_SMD:R_0805_2012Metric, F.Cu at (461.8, 48.0)
- added R159: 210R, Resistor_SMD:R_0805_2012Metric, F.Cu at (523.4, -11.2)
- added R16: 100k, Resistor_SMD:R_0603_1608Metric, F.Cu at (236.0, -28.6)
- added R160: 210R, Resistor_SMD:R_0805_2012Metric, F.Cu at (411.6, 107.2)
- added R161: 210R, Resistor_SMD:R_0805_2012Metric, F.Cu at (523.4, 18.4)
- added R162: 210R, Resistor_SMD:R_0805_2012Metric, F.Cu at (461.8, 77.6)
- added R163: 210R, Resistor_SMD:R_0805_2012Metric, F.Cu at (411.6, 136.8)
- added R164: 210R, Resistor_SMD:R_0805_2012Metric, F.Cu at (512.1, 48.0)
- added R165: 210R, Resistor_SMD:R_0805_2012Metric, F.Cu at (461.8, 107.2)
- added R166: 210R, Resistor_SMD:R_0805_2012Metric, F.Cu at (512.1, 77.6)
- added R167: 210R, Resistor_SMD:R_0805_2012Metric, F.Cu at (461.8, 136.8)
- added R168: 210R, Resistor_SMD:R_0805_2012Metric, F.Cu at (562.4, 48.0)
- added R169: 210R, Resistor_SMD:R_0805_2012Metric, F.Cu at (512.1, 107.2)
- added R17: 11R, Resistor_SMD:R_0603_1608Metric, F.Cu at (251.4, -41.7)
- added R170: 210R, Resistor_SMD:R_0805_2012Metric, F.Cu at (562.4, 77.6)
- added R171: 210R, Resistor_SMD:R_0805_2012Metric, F.Cu at (361.3, 136.8)
- added R172: 210R, Resistor_SMD:R_0805_2012Metric, F.Cu at (303.4, -70.4)
- added R173: 210R, Resistor_SMD:R_0805_2012Metric, F.Cu at (221.7, 11.5)
- added R174: 210R, Resistor_SMD:R_0805_2012Metric, F.Cu at (303.4, -40.8)
- added R175: 210R, Resistor_SMD:R_0805_2012Metric, F.Cu at (210.4, 47.5)
- added R176: 210R, Resistor_SMD:R_0805_2012Metric, F.Cu at (160.1, 77.0)
- added R177: 210R, Resistor_SMD:R_0805_2012Metric, F.Cu at (353.7, -70.4)
- added R178: 210R, Resistor_SMD:R_0805_2012Metric, F.Cu at (160.1, 106.7)
- added R179: 210R, Resistor_SMD:R_0805_2012Metric, F.Cu at (271.9, 11.5)
- added R18: DNP-4.7k, Resistor_SMD:R_0603_1608Metric, F.Cu at (217.2, -9.86)
- added R180: 210R, Resistor_SMD:R_0805_2012Metric, F.Cu at (210.4, 77.0)
- added R181: 210R, Resistor_SMD:R_0805_2012Metric, F.Cu at (353.7, -40.8)
- added R182: 210R, Resistor_SMD:R_0805_2012Metric, F.Cu at (160.1, 136.2)
- added R183: 210R, Resistor_SMD:R_0805_2012Metric, F.Cu at (260.7, 41.1)
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- renumbered S10 to SW10, S11 to SW11, S12 to SW12, S13 to SW13, S14 to SW14, S15 to SW15, S16 to SW16, S5 to SW5, S52 to SW52, S6 to SW6, S7 to SW7, S8 to SW8, S9 to SW9
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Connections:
- C4 pad 1: 5V_MCU -> Net-(C4-Pad1)
- J10 pad 1: AREF -> BTNX-1
- J10 pad 2: softpot-2 -> GND
- J11 pad 1: Net-(J11-Pad1) -> BTNX-2
- J11 pad 2: Net-(J11-Pad2) -> GND
- J12 pad 1: Net-(J12-Pad1) -> BTNX-3
- J12 pad 2: Earth -> GND
- J13 pad 1: Earth -> BTNX-7
- J13 pad 2: Net-(J13-Pad2) -> GND
- J14 pad 1: Earth -> BTNX-8
- J14 pad 2: Net-(J14-Pad2) -> GND
- J15 pad 1: Earth -> BTNX-9
- J15 pad 2: Net-(J15-Pad2) -> GND
- J16 pad 1: Earth -> BTNX-4
- J16 pad 2: Net-(J16-Pad2) -> GND
- J2 pad 1: Earth -> Net-(F2-Pad2)
- J5 pad 1: Earth -> MCU3_MISO3
- J5 pad 2: Net-(J5-Pad2) -> 5V_MCU
- J6 pad 1: Earth -> Net-(J6-Pad1)
- J7 pad 1: Earth -> Net-(J7-Pad1)
- J7 pad 2: Net-(J7-Pad2) -> GND
- J8 pad 1: Earth -> MCU2_MISO2
- J8 pad 2: Net-(J8-Pad2) -> 5V_MCU
- R21 pad 1: Net-(R21-Pad1) -> 5V_MCU
- R21 pad 2: GND -> MCU2_RST
- SW1 pad 1: Earth -> Net-(R42-Pad2)
- SW1 pad 2: button-01 -> GND
- SW17 pad 1: Earth -> BTN5
- SW17 pad 2: button-17 -> GND
- SW18 pad 1: Earth -> BTN6
- SW18 pad 2: button-18 -> GND
- SW19 pad 1: Earth -> BTN7
- SW19 pad 2: button-19 -> GND
- SW2 pad 1: Earth -> Net-(R45-Pad2)
- SW2 pad 2: button-02 -> GND
- SW20 pad 1: Earth -> BTN8
- SW20 pad 2: button-20 -> GND
- SW21 pad 1: Earth -> BTN9
- SW21 pad 2: button-21 -> GND
- SW22 pad 1: Earth -> BTN10
- SW22 pad 2: button-22 -> GND
- SW23 pad 1: Earth -> BTN11
- SW23 pad 2: button-23 -> GND
- SW24 pad 1: Earth -> BTN12
- SW24 pad 2: button-24 -> GND
- SW25 pad 1: Earth -> BTN13
- SW25 pad 2: button-25 -> GND
- SW26 pad 1: Earth -> BTN14
- SW26 pad 2: button-26 -> GND
- SW27 pad 1: Earth -> BTN15
- SW27 pad 2: button-27 -> GND
- SW28 pad 1: Earth -> BTN16
- SW28 pad 2: button-28 -> GND
- SW29 pad 1: Earth -> BTN17
- SW29 pad 2: button-29 -> GND
- SW3 pad 1: Earth -> Net-(R48-Pad2)
- SW3 pad 2: button-03 -> GND
- SW30 pad 1: Earth -> BTN18
- SW30 pad 2: button-30 -> GND
- SW31 pad 1: Earth -> BTN19
- SW31 pad 2: button-31 -> GND
- SW32 pad 1: Earth -> BTN20
- SW32 pad 2: button-32 -> GND
- SW33 pad 1: Earth -> BTN21
- SW33 pad 2: button-33 -> GND
- SW34 pad 1: Earth -> BTN22
- SW34 pad 2: button-34 -> GND
- SW35 pad 1: Earth -> BTN23
- SW35 pad 2: button-35 -> GND
- SW36 pad 1: Earth -> BTN24
- SW36 pad 2: button-36 -> GND
- SW37 pad 1: Earth -> BTN25
- SW37 pad 2: button-37 -> GND
- SW38 pad 1: Earth -> BTN26
- SW38 pad 2: button-38 -> GND
- SW39 pad 1: Earth -> BTN27
- SW39 pad 2: button-39 -> GND
- SW4 pad 1: Earth -> Net-(R51-Pad2)
- SW4 pad 2: button-04 -> GND
- SW40 pad 1: Earth -> BTN28
- SW40 pad 2: button-40 -> GND
- SW41 pad 1: Earth -> BTN29
- SW41 pad 2: button-41 -> GND
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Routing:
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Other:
- board text removed: "MIDI IN"
- board text removed: "MIDI OUT"
- board text removed: "Rainboard V0.4"
